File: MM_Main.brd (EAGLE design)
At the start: 101.4 x 83.6 mm, 68 parts, among them IC1 ULN2003AD, IC2 TB6612FNG, IC4 LD117ADT50TR, Q1 TEFT4300, Q2 TEFT4300, Q3 TEFT4300, Q4 TEFT4300, Q7 8MHz, U1 STM32F405RGT6

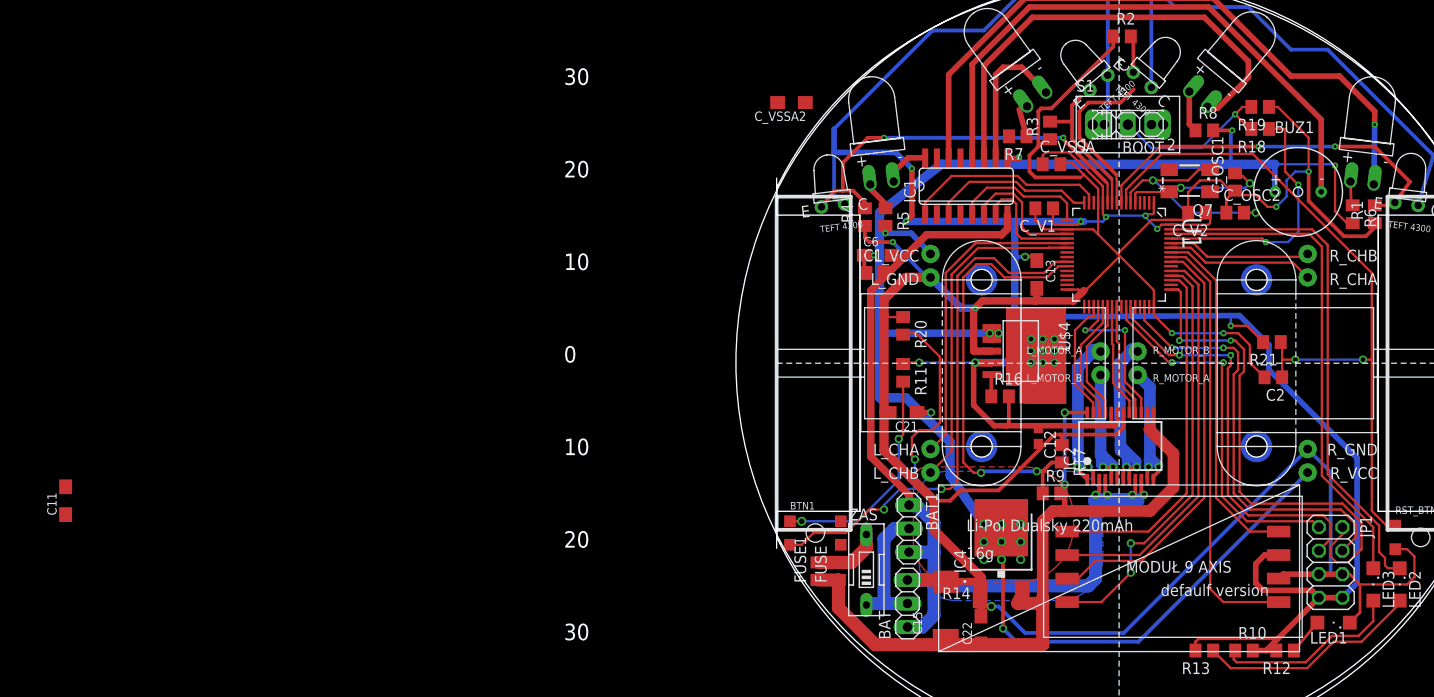
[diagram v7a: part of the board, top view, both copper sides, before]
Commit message: poprawilem zasilanie, rx/tx, obudowa stmki
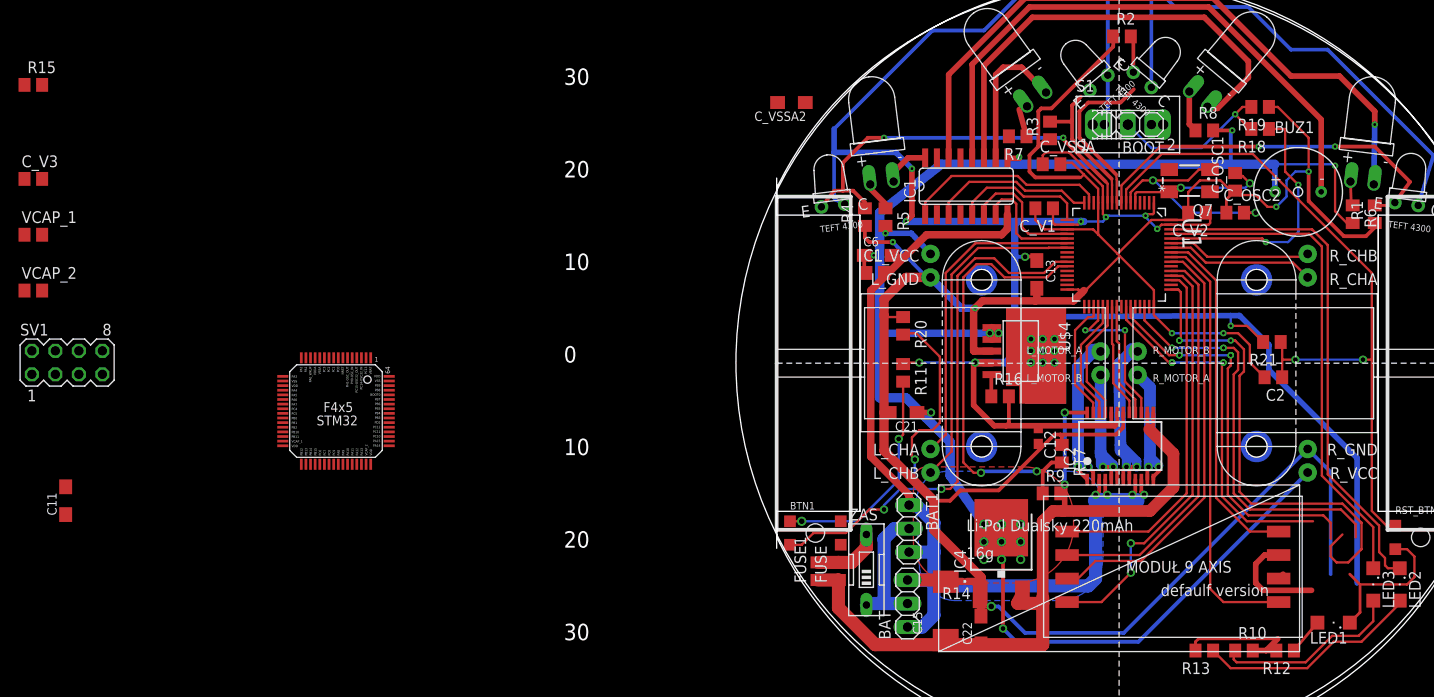
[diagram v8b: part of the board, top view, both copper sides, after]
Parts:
- removed JP1: (no value), pinhead:2X04
- added C_V3: 100n, rcl:C0805
- added R15: (no value), rcl:R0805
- added SV1: (no value), con-lstb:MA04-2
- added U$3: STM32F405/415_LQFP64, STM32F10x F4xx:STM32F405/415_LQFP64
- added VCAP_1, VCAP_2: 2,2u, rcl:C0805
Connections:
- new net N$2: R15.2, U$3.PB2
- new net N$52: U$3.PC15
- new net N$55: U$3.PC4
- new net N$57: U$3.PC5
- new net VCAP_1: U$3.VCAP_1, VCAP_1.1
- new net VCAP_2: U$3.VCAP_2, VCAP_2.1
- net +3V3: now also C_V3.1, SV1.1, SV1.2, U$3.VDDA, U$3.VDD_0, U$3.VDD_1, U$3.VDD_2, U$3.VDD_3; no longer JP1.7, JP1.8
- net ADC_L: now also U$3.PC1
- net ADC_LF: now also U$3.PC0
- net ADC_R: now also U$3.PC2
- net ADC_RF: now also U$3.PC3
- net ADC_VBAT: now also U$3.PB1
- net BOOT0: now also U$3.BOOT0
- net BTN: now also U$3.PB0
- net BT_RXD: now also SV1.6, U$3.PA9; no longer JP1.1
- net BT_TXD: now also SV1.8, U$3.PA10; no longer JP1.3
- net BUZZER: now also U$3.PA5
- net CS_A: now also U$3.PB4
- net CS_G: now also U$3.PB3
- net D_L: now also U$3.PA2
- net D_LF: now also U$3.PA1
- net D_LL: now also U$3.PC13
- net D_R: now also U$3.PA3
- net D_RF: now also U$3.PA4
- net D_RR: now also U$3.PC14
- net ENCL_A: now also U$3.PA6
- net ENCL_B: now also U$3.PA7
- net ENCR_A: now also U$3.PB6
- net ENCR_B: now also U$3.PB7
- net GND: now also C_V3.2, R15.1, SV1.3, SV1.4, U$3.VSS_0, U$3.VSS_1, VCAP_1.2, VCAP_2.2; no longer JP1.5, JP1.6
- net GNDA: now also U$3.VSSA
- net INT_A: now also U$3.PB5
- net LED1: now also U$3.PB9
- net LED2: now also U$3.PB8
- net MISO: now also U$3.PC11
- net ML_IN1: now also U$3.PC6
- net ML_IN2: now also U$3.PC7
- net ML_PWM: now also U$3.PB14
- net MOSI: now also U$3.PC12
- net MR_IN1: now also U$3.PC8
- net MR_IN2: now also U$3.PC9
- net MR_PWM: now also U$3.PB15
- net OSC_IN: now also U$3.PH0
- net OSC_OUT: now also U$3.PH1
- net RST: now also U$3.NRST
- net SCLK: now also U$3.PC10
- net SWCLK: now also SV1.7, U$3.PA14; no longer JP1.2
- net SWDIO: now also SV1.5, U$3.PA13; no longer JP1.4
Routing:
- net +3V3: track 349.5 -> 337.3 mm
- net GND: track 335.4 -> 326.9 mm
- net SWDIO: track 46.5 -> 44.4 mm
- net BT_TXD: track 44.7 -> 43.0 mm
- net BT_RXD: track 40.2 -> 39.3 mm
- net SWCLK: track 54.8 -> 54.1 mm
